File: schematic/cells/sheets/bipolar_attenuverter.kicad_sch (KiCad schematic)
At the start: 9 parts, among them J708 PORT_LOAD, J709 PORT_LOAD, U707 OPA4196IDR

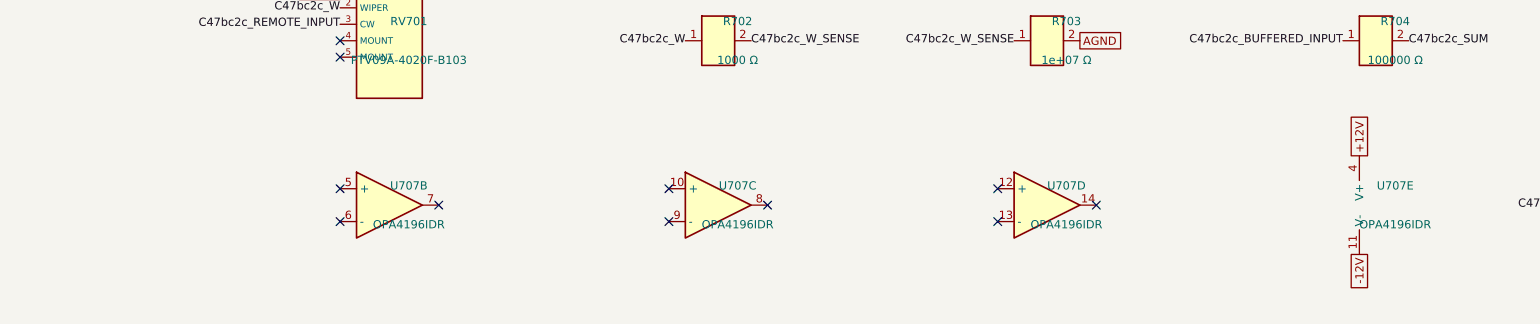
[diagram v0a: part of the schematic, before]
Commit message: Close master schematic integration gates
Audit locked panel coverage, netlist parity, sensitive islands and all active units; terminate spare cells, refresh evidence, and record rail budget overshoot and draft exports.
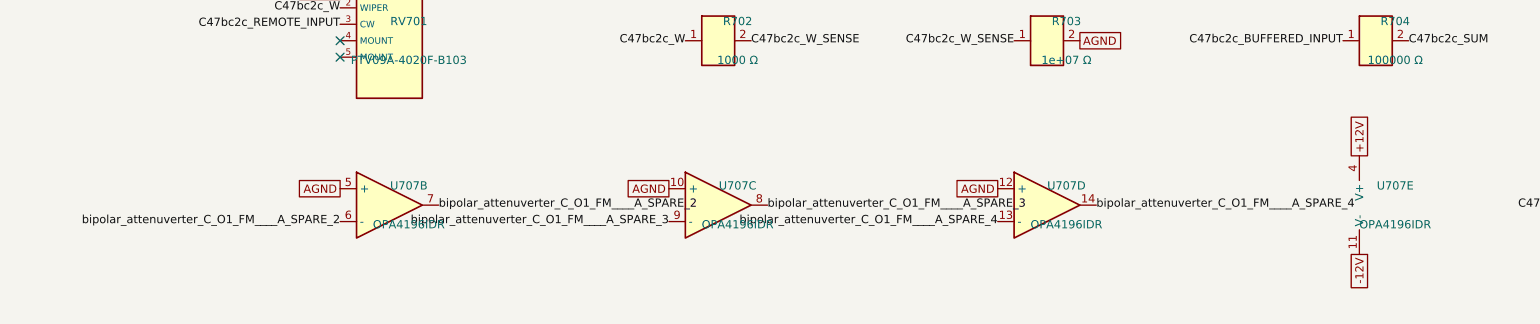
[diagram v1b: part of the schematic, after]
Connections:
- net AGND: now also U707.10 (+), U707.12 (+), U707.5 (+)
- net bipolar_attenuverter_C_O1_FM____A_SPARE_4: now reaches U707.13 (-)
- net bipolar_attenuverter_C_O1_FM____A_SPARE_4: now also U707.14
- net bipolar_attenuverter_C_O1_FM____A_SPARE_3: now reaches U707.8
- net bipolar_attenuverter_C_O1_FM____A_SPARE_3: now also U707.9 (-)
- net bipolar_attenuverter_C_O1_FM____A_SPARE_2: now reaches U707.6 (-)
- net bipolar_attenuverter_C_O1_FM____A_SPARE_2: now also U707.7
- no-connect marks 13 -> 4
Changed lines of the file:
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@@
     ))
   )
-  (no_connect (at 43.18 73.66))
-  (no_connect (at 43.18 78.74))
-  (no_connect (at 58.42 76.2))
+  (global_label "AGND" (shape passive) (at 43.18 73.66 0) (effects (font (size 1.27 1.27)) (justify right)))
+  (label "bipolar_attenuverter_C_O1_FM____A_SPARE_2" (at 43.18 78.74 0) (effects (font (size 1.27 1.27)) (justify right)))
+  (label "bipolar_attenuverter_C_O1_FM____A_SPARE_2" (at 58.42 76.2 180) (effects (font (size 1.27 1.27)) (justify left)))
   (symbol (lib_id "zudo-osc-hole-field:OPA4196IDR") (at 101.6 76.2 0) (unit 3)
     (exclude_from_sim no) (in_bom yes) (on_board yes) (dnp no)
@@
     ))
   )
-  (no_connect (at 109.22 76.2))
-  (no_connect (at 93.98 78.74))
-  (no_connect (at 93.98 73.66))
+  (label "bipolar_attenuverter_C_O1_FM____A_SPARE_3" (at 109.22 76.2 180) (effects (font (size 1.27 1.27)) (justify left)))
+  (label "bipolar_attenuverter_C_O1_FM____A_SPARE_3" (at 93.98 78.74 0) (effects (font (size 1.27 1.27)) (justify right)))
+  (global_label "AGND" (shape passive) (at 93.98 73.66 0) (effects (font (size 1.27 1.27)) (justify right)))
   (symbol (lib_id "zudo-osc-hole-field:OPA4196IDR") (at 152.4 76.2 0) (unit 4)
     (exclude_from_sim no) (in_bom yes) (on_board yes) (dnp no)
@@
     ))
   )
-  (no_connect (at 144.78 73.66))
-  (no_connect (at 144.78 78.74))
-  (no_connect (at 160.02 76.2))
+  (global_label "AGND" (shape passive) (at 144.78 73.66 0) (effects (font (size 1.27 1.27)) (justify right)))
+  (label "bipolar_attenuverter_C_O1_FM____A_SPARE_4" (at 144.78 78.74 0) (effects (font (size 1.27 1.27)) (justify right)))
+  (label "bipolar_attenuverter_C_O1_FM____A_SPARE_4" (at 160.02 76.2 180) (effects (font (size 1.27 1.27)) (justify left)))
   (symbol (lib_id "zudo-osc-hole-field:OPA4196IDR") (at 203.2 76.2 0) (unit 5)
     (exclude_from_sim no) (in_bom yes) (on_board yes) (dnp no)
